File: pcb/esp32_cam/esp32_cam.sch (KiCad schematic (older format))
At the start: 45 parts, among them CN1 ESP32CAM_P1, CN2 ESP-PSRAM32, CN3 Cam_Connector, CN4 ESP32CAM_P2, CN5 microSD_esp32Cam, Q1 S8050, Q2 PMOS, SW1 SWITCH, U1 ESP32-S(CAM), U2 AMS1117, U4 XC6206-2,8V, U5 XC6206-1,2V

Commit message: correcciones de esquematico y se agrega y completa  información
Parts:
- added H1, H2, H3, H4: MountingHole, MountingHole:MountingHole_2.5mm, symbol Mechanical:MountingHole
- SW1: footprint Button_Switch_SMD:SW_SPST_Omron_B3FS-101xP -> Button_Switch_SMD:SW_SPST_B3U-1000P; symbol Switch:SW_DPST -> Switch:SW_DPST_x2
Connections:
- net GND: no longer SW1.4
- net at C3.2, R2.2, SW1.1 (A)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: no longer SW1.3
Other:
- note added: "ETAPA PRINCIPAL (ESP32)"
- note added: "FUENTE DE ALIMENTACIÓN"
- note added: "INDICADOR LED"
- note added: "MEMORIA MICRO SD"
- note added: "MOUNTING HOLES"
- note added: "PULL UPS"
- moved on the sheet: C10, C11, C2, C4, C5, C6, C7, C8, C9, D2, Q1, Q2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

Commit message: se sube primera versión del PCB
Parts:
- CN1, CN4: footprint Connector_PinHeader_1.27mm:PinHeader_1x08_P1.27mm_Vertical -> Connector_PinHeader_2.54mm:PinHeader_1x08_P2.54mm_Vertical
- H3, H4: footprint MountingHole:MountingHole_2.5mm -> MountingHole:MountingHole_2.1mm
- Q1: footprint Package_TO_SOT_SMD:SC-59_Handsoldering -> Package_TO_SOT_SMD:SOT-23
- Q2: footprint Package_TO_SOT_SMD:SOT-89-3_Handsoldering -> Package_TO_SOT_SMD:SOT-23
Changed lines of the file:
@@
 encoding utf-8
 Sheet 1 1
-Title "ESP32-CAM"
+Title "Réplica ESP32-CAM"
 Date "2021-07-02"
 Rev "V1.0"
@@
 F 0 "CN1" H 2050 4000 50  0000 C CNN
 F 1 "ESP32CAM_P1" H 2450 3500 50  0000 C CNN
-F 2 "Connector_PinHeader_1.27mm:PinHeader_1x08_P1.27mm_Vertical" V 2450 4025 50  0001 C CNN
+F 2 "Connector_PinHeader_2.54mm:PinHeader_1x08_P2.54mm_Vertical" V 2450 4025 50  0001 C CNN
 F 3 "~" V 2450 4025 50  0001 C CNN
 	1    2450 4000
@@
 F 0 "CN4" H 6907 5717 50  0000 C CNN
 F 1 "ESP32CAM_P2" H 6907 5626 50  0000 C CNN
-F 2 "Connector_PinHeader_1.27mm:PinHeader_1x08_P1.27mm_Vertical" V 6850 5075 50  0001 C CNN
+F 2 "Connector_PinHeader_2.54mm:PinHeader_1x08_P2.54mm_Vertical" V 6850 5075 50  0001 C CNN
 F 3 "~" V 6850 5075 50  0001 C CNN
 	1    6850 5050
@@
 F 0 "Q1" H 10591 2996 50  0000 L CNN
 F 1 "S8050" H 10591 2905 50  0000 L CNN
-F 2 "Package_TO_SOT_SMD:SC-59_Handsoldering" H 10600 2875 50  0001 L CIN
+F 2 "Package_TO_SOT_SMD:SOT-23" H 10600 2875 50  0001 L CIN
 F 3 "http://www.unisonic.com.tw/datasheet/S8050.pdf" H 10400 2950 50  0001 L CNN
 	1    10400 2950
@@
 F 0 "Q2" V 3992 6150 50  0000 C CNN
 F 1 "PMOS" V 3901 6150 50  0000 C CNN
-F 2 "Package_TO_SOT_SMD:SOT-89-3_Handsoldering" H 3850 6250 50  0001 C CNN
+F 2 "Package_TO_SOT_SMD:SOT-23" H 3850 6250 50  0001 C CNN
 F 3 "~" H 3650 6150 50  0001 C CNN
 	1    3650 6150
@@
 F 0 "H3" H 8100 3246 50  0000 L CNN
 F 1 "MountingHole" H 8100 3155 50  0000 L CNN
-F 2 "MountingHole:MountingHole_2.5mm" H 8000 3200 50  0001 C CNN
+F 2 "MountingHole:MountingHole_2.1mm" H 8000 3200 50  0001 C CNN
 F 3 "~" H 8000 3200 50  0001 C CNN
 	1    8000 3200
@@
 F 0 "H4" H 8100 3546 50  0000 L CNN
 F 1 "MountingHole" H 8100 3455 50  0000 L CNN
-F 2 "MountingHole:MountingHole_2.5mm" H 8000 3500 50  0001 C CNN
+F 2 "MountingHole:MountingHole_2.1mm" H 8000 3500 50  0001 C CNN
 F 3 "~" H 8000 3500 50  0001 C CNN
 	1    8000 3500

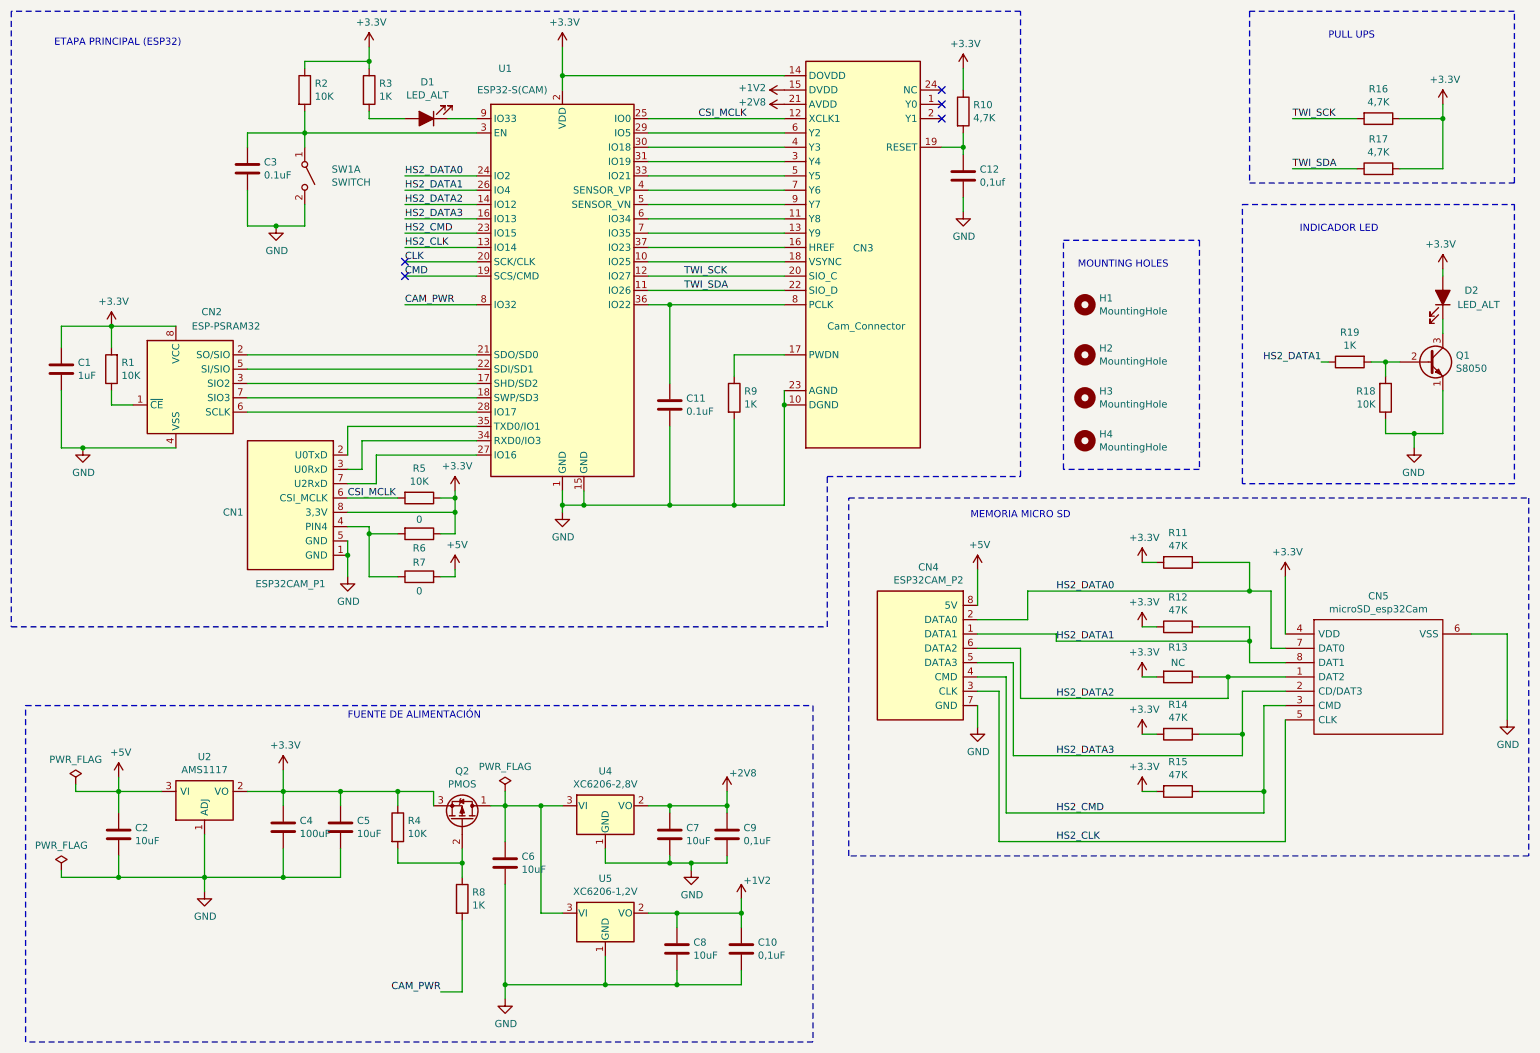
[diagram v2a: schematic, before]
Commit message: se sube versión final y se agrega documentación
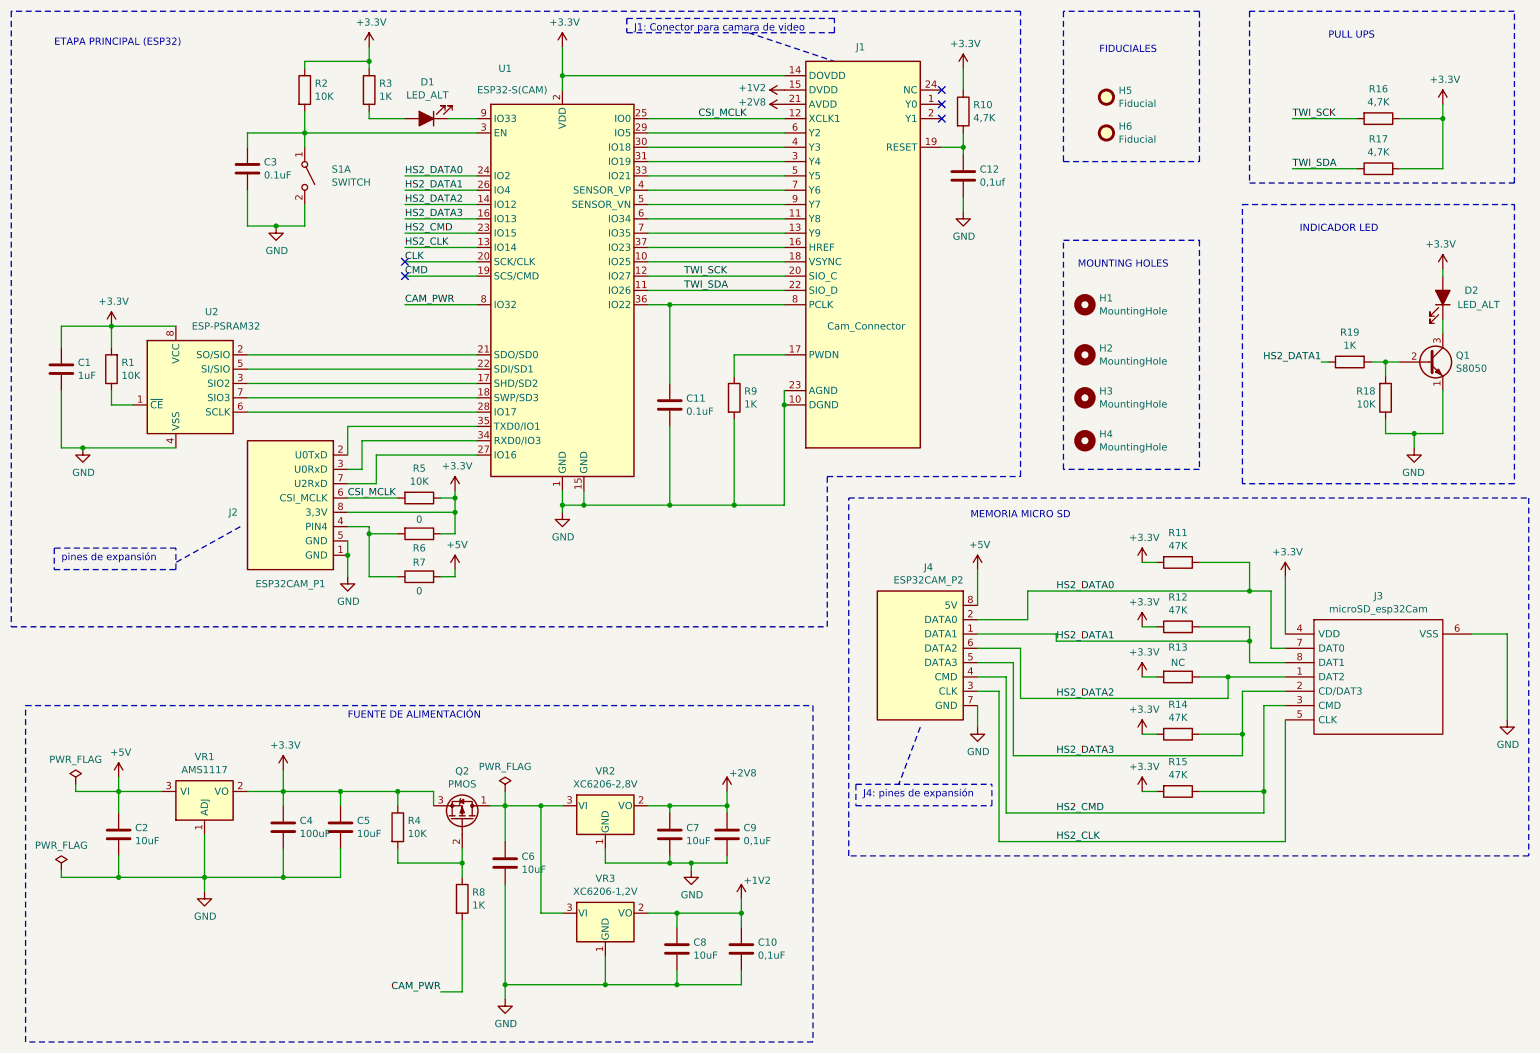
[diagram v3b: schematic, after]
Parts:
- added H5, H6: Fiducial, Fiducial:Fiducial_0.5mm_Mask1mm, symbol Mechanical:Fiducial
- renumbered CN3 to J1, CN1 to J2, CN5 to J3, CN4 to J4, SW1 to S1, CN2 to U2, U2 to VR1, U4 to VR2, U5 to VR3
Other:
- note added: "FIDUCIALES"
- note added: "J1: Conector para camara de video"
- note added: "J4: pines de expansión"
- note added: "pines de expansión"
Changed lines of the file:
@@
 $EndComp
 $Comp
-L DM3AT-SF-PEJM5:microSD_esp32Cam CN5
+L DM3AT-SF-PEJM5:microSD_esp32Cam J3
 U 1 1 611218DA
 P 9400 4850
-F 0 "CN5" H 10050 5115 50  0000 C CNN
+F 0 "J3" H 10050 5115 50  0000 C CNN
 F 1 "microSD_esp32Cam" H 10050 5024 50  0000 C CNN
 F 2 "DM3AT-SF-PEJM5:DM3ATSFPEJM5" H 10550 4950 50  0001 L CNN
@@
 HS2_CLK
 $Comp
-L Cam_con:ESP32CAM_P1 CN1
+L Cam_con:ESP32CAM_P1 J2
 U 1 1 611C9FDF
 P 2450 4000
-F 0 "CN1" H 2050 4000 50  0000 C CNN
+F 0 "J2" H 2050 4000 50  0000 C CNN
 F 1 "ESP32CAM_P1" H 2450 3500 50  0000 C CNN
 F 2 "Connector_PinHeader_2.54mm:PinHeader_1x08_P2.54mm_Vertical" V 2450 4025 50  0001 C CNN
-F 3 "~" V 2450 4025 50  0001 C CNN
+F 3 "https://ar.mouser.com/datasheet/2/35/12034-strip-line-header-337594.pdf" V 2450 4025 50  0001 C CNN
 	1    2450 4000
 	1    0    0    -1
 $EndComp
 $Comp
-L Cam_con:Cam_Connector CN3
+L Cam_con:Cam_Connector J1
 U 1 1 611CD372
 P 6200 4150
-F 0 "CN3" H 6380 6146 50  0000 L CNN
+F 0 "J1" H 6400 7550 50  0000 L CNN
 F 1 "Cam_Connector" H 6200 5600 50  0000 L CNN
 F 2 "Connector_FFC-FPC:TE_2-1734839-4_1x24-1MP_P0.5mm_Horizontal" H 6200 4200 50  0001 C CNN
-F 3 " ~" H 6200 4200 50  0001 C CNN
+F 3 "https://ar.mouser.com/datasheet/2/185/FH12_CL0586_0704_0_55_2d-1614775.pdf" H 6200 4200 50  0001 C CNN
 	1    6200 4150
 	1    0    0    -1
 $EndComp
 $Comp
-L Cam_con:ESP32CAM_P2 CN4
+L Cam_con:ESP32CAM_P2 J4
 U 1 1 611FA2E7
 P 6850 5050
-F 0 "CN4" H 6907 5717 50  0000 C CNN
+F 0 "J4" H 6907 5717 50  0000 C CNN
 F 1 "ESP32CAM_P2" H 6907 5626 50  0000 C CNN
 F 2 "Connector_PinHeader_2.54mm:PinHeader_1x08_P2.54mm_Vertical" V 6850 5075 50  0001 C CNN
-F 3 "~" V 6850 5075 50  0001 C CNN
+F 3 "https://ar.mouser.com/datasheet/2/35/12034-strip-line-header-337594.pdf" V 6850 5075 50  0001 C CNN
 	1    6850 5050
 	1    0    0    -1
@@
 $EndComp
 $Comp
-L Regulator_Linear:AMS1117 U2
+L Regulator_Linear:AMS1117 VR1
 U 1 1 6143DB27
 P 1850 5950
-F 0 "U2" H 1850 6192 50  0000 C CNN
+F 0 "VR1" H 1850 6192 50  0000 C CNN
 F 1 "AMS1117" H 1850 6101 50  0000 C CNN
 F 2 "Package_TO_SOT_SMD:SOT-223-3_TabPin2" H 1850 6150 50  0001 C CNN
@@
 $EndComp
 $Comp
-L Regulator_Linear:XC6206PxxxMR U4
+L Regulator_Linear:XC6206PxxxMR VR2
 U 1 1 6143E22A
 P 4650 6050
-F 0 "U4" H 4650 6292 50  0000 C CNN
+F 0 "VR2" H 4650 6292 50  0000 C CNN
 F 1 "XC6206-2,8V" H 4650 6201 50  0000 C CNN
 F 2 "Package_TO_SOT_SMD:SOT-23" H 4650 6275 50  0001 C CIN
@@
 $EndComp
 $Comp
-L Regulator_Linear:XC6206PxxxMR U5
+L Regulator_Linear:XC6206PxxxMR VR3
 U 1 1 6143EC5C
 P 4650 6800
-F 0 "U5" H 4650 7042 50  0000 C CNN
+F 0 "VR3" H 4650 7042 50  0000 C CNN
 F 1 "XC6206-1,2V" H 4650 6951 50  0000 C CNN
 F 2 "Package_TO_SOT_SMD:SOT-23" H 4650 7025 50  0001 C CIN
@@
 	3000 4150 3000 4450
 $Comp
-L PSRAM(ESP32CAM):ESP-PSRAM32 CN2
+L PSRAM(ESP32CAM):ESP-PSRAM32 U2
 U 1 1 61775F15
 P 1750 3200
-F 0 "CN2" H 1900 3800 50  0000 C CNN
+F 0 "U2" H 1900 3800 50  0000 C CNN
 F 1 "ESP-PSRAM32" H 2000 3700 50  0000 C CNN
 F 2 "Package_SO:SOIC-8_3.9x4.9mm_P1.27mm" H 1750 2600 50  0001 C CNN
@@
 	5900 3250 5900 3950
 $Comp
-L Switch:SW_DPST_x2 SW1
+L Switch:SW_DPST_x2 S1
 U 1 1 61249965
 P 2550 1650
-F 0 "SW1" V 2504 1838 50  0000 L CNN
+F 0 "S1" V 2504 1838 50  0000 L CNN
 F 1 "SWITCH" V 2595 1838 50  0000 L CNN
 F 2 "Button_Switch_SMD:SW_SPST_B3U-1000P" H 2550 1650 50  0001 C CNN
@@
 Wire Wire Line
 	2550 1350 3750 1350
+$Comp
+L Mechanical:Fiducial H5
+U 1 1 611CB90A
+P 8150 1100
+F 0 "H5" H 8235 1146 50  0000 L CNN
+F 1 "Fiducial" H 8235 1055 50  0000 L CNN
+F 2 "Fiducial:Fiducial_0.5mm_Mask1mm" H 8150 1100 50  0001 C CNN
+F 3 "~" H 8150 1100 50  0001 C CNN
+	1    8150 1100
+	1    0    0    -1
+$EndComp
+$Comp
+L Mechanical:Fiducial H6
+U 1 1 611CDC21
+P 8150 1350
+F 0 "H6" H 8235 1396 50  0000 L CNN
+F 1 "Fiducial" H 8235 1305 50  0000 L CNN
+F 2 "Fiducial:Fiducial_0.5mm_Mask1mm" H 8150 1350 50  0001 C CNN
+F 3 "~" H 8150 1350 50  0001 C CNN
+	1    8150 1350
+	1    0    0    -1
+$EndComp
+Text Notes 8100 800  0    50   ~ 0
+FIDUCIALES
+Wire Notes Line
+	7850 1550 8800 1550
+Wire Notes Line
+	8800 1550 8800 500
+Wire Notes Line
+	8800 500  7850 500
+Wire Notes Line
+	7850 500  7850 1550
+Text Notes 4850 650  0    50   ~ 0
+J1: Conector para camara de video
+Wire Notes Line
+	6250 650  6250 550
+Wire Notes Line
+	6250 550  4800 550
+Wire Notes Line
+	4800 550  4800 650
+Wire Notes Line
+	4800 650  6250 650
+Wire Notes Line
+	5650 650  6250 850
+Text Notes 6450 6000 0    50   ~ 0
+J4: pines de expansión
+Wire Notes Line
+	7350 6050 7350 5900
+Wire Notes Line
+	6400 5900 6400 6050
+Wire Notes Line
+	6400 6050 7350 6050
+Wire Notes Line
+	6400 5900 7350 5900
+Wire Notes Line
+	6850 5500 6700 5900
+Text Notes 850  4350 0    50   ~ 0
+pines de expansión
+Wire Notes Line
+	800  4400 1650 4400
+Wire Notes Line
+	1650 4400 1650 4250
+Wire Notes Line
+	1650 4250 800  4250
+Wire Notes Line
+	800  4250 800  4400
+Wire Notes Line
+	2100 4100 1650 4350
 $EndSCHEMATC

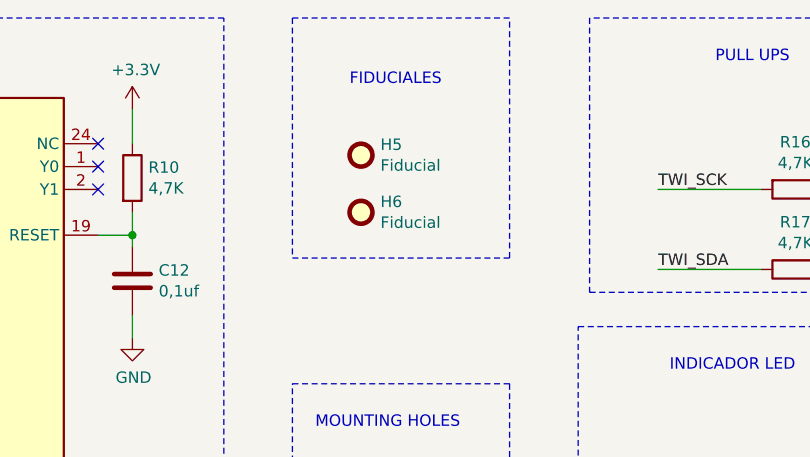
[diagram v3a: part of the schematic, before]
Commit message: se crea la carpeta shapes3D
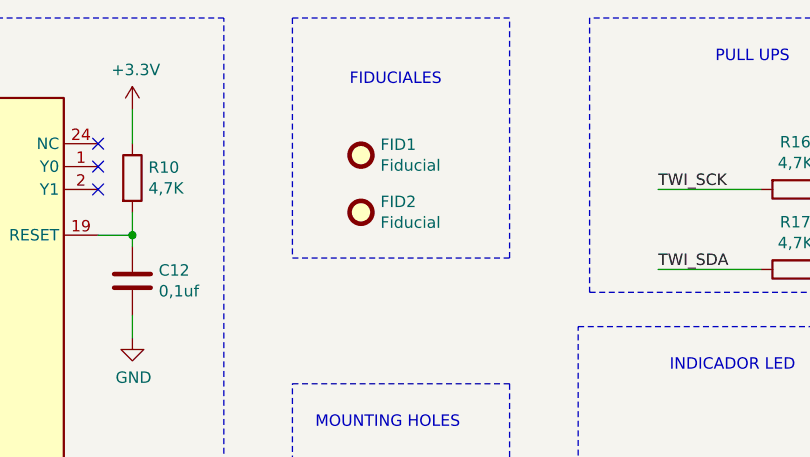
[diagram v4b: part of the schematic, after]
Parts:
- renumbered H5 to FID1, H6 to FID2
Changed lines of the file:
@@
 	2550 1350 3750 1350
 $Comp
-L Mechanical:Fiducial H5
+L Mechanical:Fiducial FID1
 U 1 1 611CB90A
 P 8150 1100
-F 0 "H5" H 8235 1146 50  0000 L CNN
+F 0 "FID1" H 8235 1146 50  0000 L CNN
 F 1 "Fiducial" H 8235 1055 50  0000 L CNN
 F 2 "Fiducial:Fiducial_0.5mm_Mask1mm" H 8150 1100 50  0001 C CNN
@@
 $EndComp
 $Comp
-L Mechanical:Fiducial H6
+L Mechanical:Fiducial FID2
 U 1 1 611CDC21
 P 8150 1350
-F 0 "H6" H 8235 1396 50  0000 L CNN
+F 0 "FID2" H 8235 1396 50  0000 L CNN
 F 1 "Fiducial" H 8235 1305 50  0000 L CNN
 F 2 "Fiducial:Fiducial_0.5mm_Mask1mm" H 8150 1350 50  0001 C CNN
